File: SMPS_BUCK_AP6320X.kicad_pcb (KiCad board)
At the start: 2 copper layers, 14.4 x 14.6 mm, 12 parts, among them U2 AP63205WU-7

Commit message: New layout.
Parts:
- added D1: LTST-C190KFKT, kicad_lib:Lite-On_LTST-C190KFKT, F.Cu at (159.2, 118.2)
- added J1: 61300411121, kicad_lib:Würth_Elektronik_61300411121, B.Cu at (154.3, 122.8)
- added R3: 10 kΩ, kicad_lib:YAGEO_RC0603FR-070RL, F.Cu at (157.6, 118.2)
- added R4: 10 kΩ, kicad_lib:YAGEO_RC0603FR-070RL, F.Cu at (149.6, 116.6)
- added REF**: Untitled, kicad_lib:agro_logo_10mm, B.Cu at (155.4, 114.6)
- moved Cb4 11.8 mm to (158.4, 120.6), turned to 180 degrees
- moved Cb2 11.1 mm to (155.2, 120.6), turned to 0 degrees
- moved Cb3 8.84 mm to (155.2, 119.0), turned to 0 degrees
- moved Cd3 7.24 mm to (155.2, 117.4), turned to 0 degrees
- moved R2 4.28 mm to (152.6, 111.8)
- moved R1 3.26 mm to (150.2, 112.6), turned to 180 degrees
- moved Cd1 1.61 mm to (154.2, 111.8), turned to 90 degrees
- moved Cd4 1.00 mm to (150.2, 111.0), turned to 180 degrees
- moved L1 0.63 mm to (157.2, 114.2), turned to 0 degrees
- moved U2 0.60 mm to (153.0, 115.0)
- moved Cb1 0.10 mm to (152.0, 117.4)
- moved Cd2 0.10 mm to (152.0, 119.0)
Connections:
- net /OUT renamed /VOUT
- U2 pad 2: unconnected-(U2-EN-Pad2) -> /EN
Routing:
- net /EN: track 0.00 -> 10.4 mm
- net /VOUT: track 14.3 -> 22.3 mm, vias 0 -> 2
- net /VIN: track 3.05 -> 7.76 mm
- net Net-(U2-SW): track 3.89 -> 0.00 mm
- net Net-(D1-PadA): track 0.00 -> 1.60 mm
- net /FB: track 6.15 -> 4.94 mm
- net Net-(U2-BST): track 2.65 -> 1.49 mm
- net GND: vias 2 -> 1
- added copper zone on F.Cu, net /VOUT
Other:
- board size 14.4 x 14.6 mm -> 12.6 x 14.6 mm

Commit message: New layout.
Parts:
- removed Cb1: 10 uF, kicad_lib:Samsung_Electro-Mechanics_CL10B104JB8NNNC
- removed REF**: Untitled, kicad_lib:agro_logo_10mm
- added C1: 10 uF, kicad_lib:Samsung_Electro-Mechanics_CL10B104JB8NNNC, F.Cu at (152.0, 117.4)
- added C2: 1 uF, kicad_lib:Samsung_Electro-Mechanics_CL10B104JB8NNNC, F.Cu at (152.0, 120.6)
- R1: value 10 kΩ -> 0 Ω
- R3: value 10 kΩ -> 1 kΩ
- moved Cd4 1.60 mm to (150.2, 112.6)
- moved R1 1.60 mm to (150.2, 111.0)
- turned R3 to 90 degrees
- renumbered U2 to U1
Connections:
- R3 pad 1: Net-(D1-PadA) -> /VOUT
- R3 pad 2: /VOUT -> Net-(D1-PadA)
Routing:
- net /VOUT: track 22.3 -> 25.5 mm
- net GND: vias 1 -> 10
- removed copper zone on F.Cu, net /VOUT

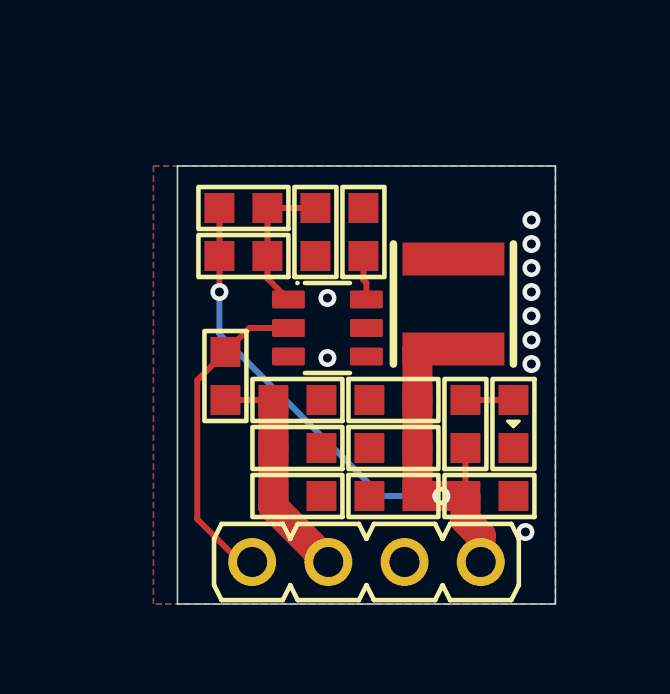
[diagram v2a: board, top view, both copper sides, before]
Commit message: Changed inductor and layout.
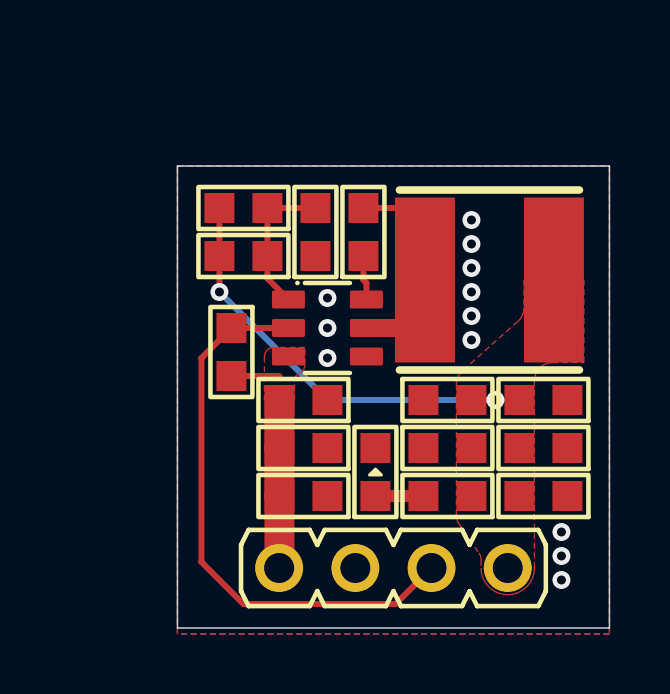
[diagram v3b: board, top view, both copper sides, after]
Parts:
- removed Cb4: 10 uF, kicad_lib:Samsung_Electro-Mechanics_CL10B104JB8NNNC
- added Cb3: 10 uF, kicad_lib:Samsung_Electro-Mechanics_CL10B104JB8NNNC, F.Cu at (160.2, 117.4)
- added Cf1: 100 pF, kicad_lib:Samsung_Electro-Mechanics_CL10B104JB8NNNC, F.Cu at (150.2, 112.6)
- L1: value Abracon LLC ASPI-4030S-6R8M-T -> Abracon LLC ASPI-0628-6R8M-T1; footprint kicad_lib:Abracon_LLC_ASPI-4030S-6R8M-T -> kicad_lib:Abracon_LLC_ASPI-0628-6R8M-T1
- moved Cd4 12.8 mm to (160.2, 120.6)
- moved Cb1 5.25 mm to (160.2, 119.0), turned to 180 degrees
- moved D1 4.87 mm to (154.6, 119.8), turned to 90 degrees
- moved R3 2.47 mm to (157.0, 120.6), turned to 180 degrees
- moved Cb2 1.80 mm to (157.0, 119.0)
- moved Cd3 1.80 mm to (157.0, 117.4)
- moved L1 1.44 mm to (158.4, 113.4), turned to 90 degrees
- moved J1 0.92 mm to (155.2, 123.0)
- moved R4 0.82 mm to (149.8, 115.8)
- moved Ca1 0.20 mm to (152.2, 117.4)
- moved Cd2 0.20 mm to (152.2, 119.0)
- moved Ce1 0.20 mm to (152.2, 120.6)
- renumbered C1 to Ca1, Cb2 to Cb1, Cb3 to Cb2, C2 to Ce1
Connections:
- Cd4 pad 1: /FB -> GND
- J1 pad 1: /EN -> /VIN
- J1 pad 2: /VIN -> GND
- J1 pad 3: GND -> /EN
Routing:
- net /VOUT: track 25.5 -> 13.5 mm
- net /EN: track 10.4 -> 18.9 mm
- net Net-(U1-SW): track 0.00 -> 5.60 mm
- net /VIN: track 7.76 -> 7.19 mm
- net GND: vias 10 -> 12
- added copper zone on F.Cu, net /VIN
- added copper zone on F.Cu, net /VOUT
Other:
- board size 12.6 x 14.6 mm -> 14.4 x 15.4 mm

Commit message: Added README file and PCB logos.
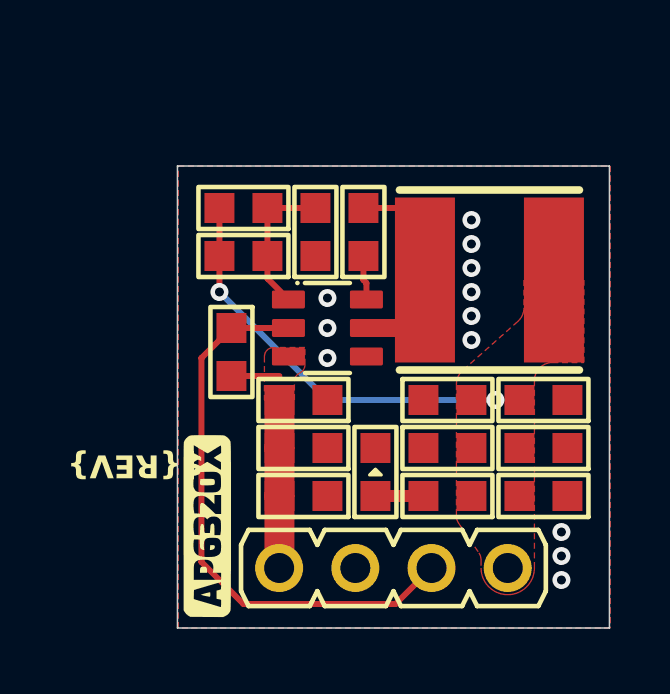
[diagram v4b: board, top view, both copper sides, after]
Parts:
- added G***: LOGO, LOGO, F.Cu at (149.0, 121.6)
- added G***: LOGO, LOGO, B.Cu at (151.0, 118.8)
- added G***: LOGO, LOGO, B.Cu at (151.0, 116.0)
- added REF**: Untitled, kicad_lib:agro_logo_5mm, B.Cu at (151.2, 112.2)
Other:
- board text added: "${REV}"
